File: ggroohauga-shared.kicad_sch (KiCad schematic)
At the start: 13 parts

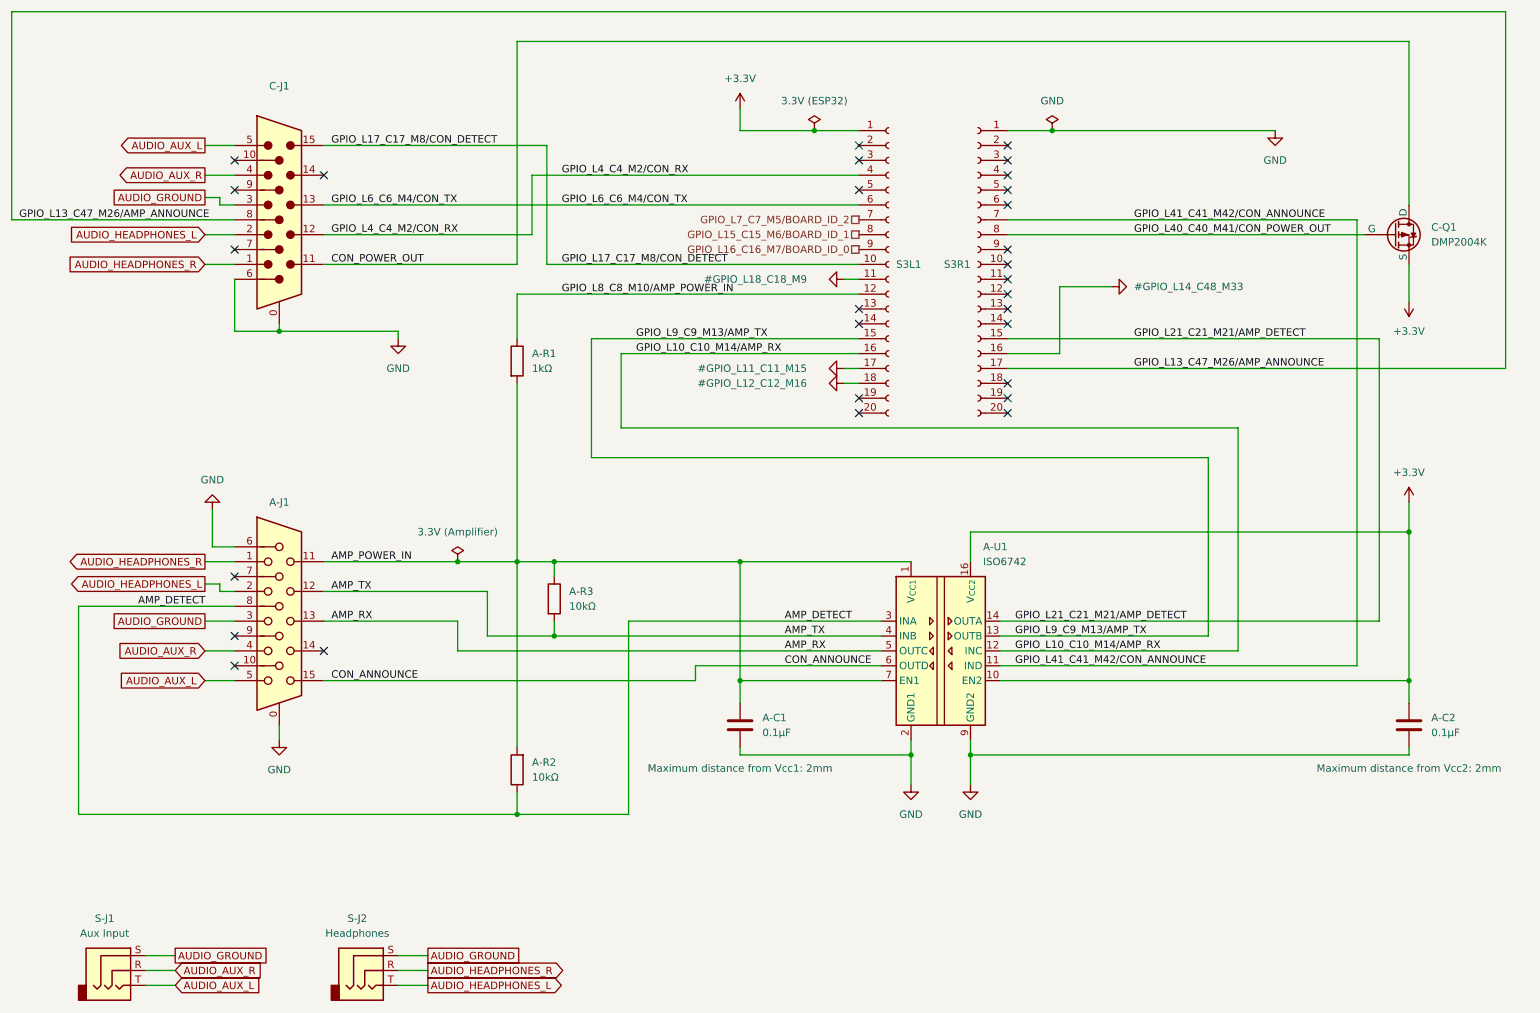
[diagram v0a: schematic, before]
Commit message: Indicate active low signals on the schematic
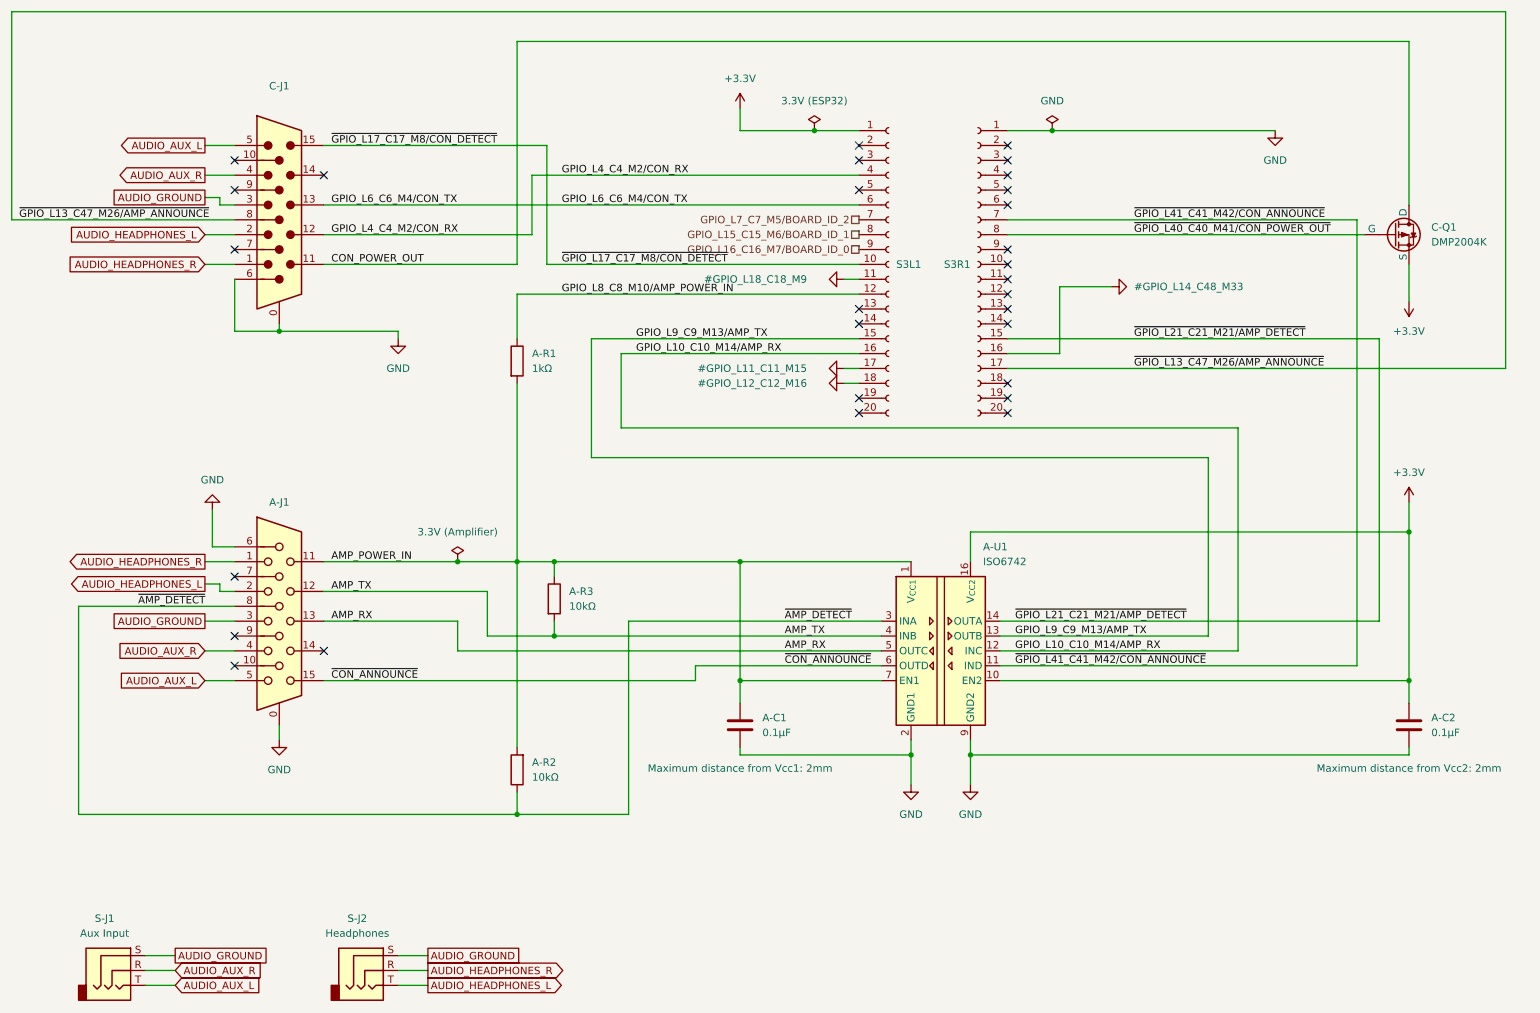
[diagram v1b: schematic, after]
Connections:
- net AMP_DETECT renamed ~{AMP_DETECT}
- net CON_ANNOUNCE renamed ~{CON_ANNOUNCE}
- net GPIO_L13_C47_M26/AMP_ANNOUNCE renamed ~{GPIO_L13_C47_M26/AMP_ANNOUNCE}
- net GPIO_L17_C17_M8/CON_DETECT renamed ~{GPIO_L17_C17_M8/CON_DETECT}
- net GPIO_L21_C21_M21/AMP_DETECT renamed ~{GPIO_L21_C21_M21/AMP_DETECT}
- net GPIO_L40_C40_M41/CON_POWER_OUT renamed ~{GPIO_L40_C40_M41/CON_POWER_OUT}
- net GPIO_L41_C41_M42/CON_ANNOUNCE renamed ~{GPIO_L41_C41_M42/CON_ANNOUNCE}
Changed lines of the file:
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@@
 		)
 	)
-	(label "GPIO_L17_C17_M8{slash}CON_DETECT"
+	(label "~{GPIO_L17_C17_M8{slash}CON_DETECT}"
 		(at 72.39 40.64 0)
 		(effects
@@
 		)
 	)
-	(label "AMP_DETECT"
+	(label "~{AMP_DETECT}"
 		(at 39.37 119.38 0)
 		(effects
@@
 		)
 	)
-	(label "CON_ANNOUNCE"
+	(label "~{CON_ANNOUNCE}"
 		(at 72.39 132.08 0)
 		(effects
@@
 		)
 	)
-	(label "GPIO_L13_C47_M26{slash}AMP_ANNOUNCE"
+	(label "~{GPIO_L13_C47_M26{slash}AMP_ANNOUNCE}"
 		(at 19.05 53.34 0)
 		(effects
@@
 		)
 	)
-	(label "AMP_DETECT"
+	(label "~{AMP_DETECT}"
 		(at 149.86 121.92 0)
 		(effects
@@
 		)
 	)
-	(label "CON_ANNOUNCE"
+	(label "~{CON_ANNOUNCE}"
 		(at 149.86 129.54 0)
 		(effects
@@
 		)
 	)
-	(label "GPIO_L13_C47_M26{slash}AMP_ANNOUNCE"
+	(label "~{GPIO_L13_C47_M26{slash}AMP_ANNOUNCE}"
 		(at 209.55 78.74 0)
 		(effects
@@
 		)
 	)
-	(label "GPIO_L21_C21_M21{slash}AMP_DETECT"
+	(label "~{GPIO_L21_C21_M21{slash}AMP_DETECT}"
 		(at 209.55 73.66 0)
 		(effects
@@
 		)
 	)
-	(label "GPIO_L17_C17_M8{slash}CON_DETECT"
+	(label "~{GPIO_L17_C17_M8{slash}CON_DETECT}"
 		(at 111.76 60.96 0)
 		(effects
@@
 		)
 	)
-	(label "GPIO_L21_C21_M21{slash}AMP_DETECT"
+	(label "~{GPIO_L21_C21_M21{slash}AMP_DETECT}"
 		(at 189.23 121.92 0)
 		(effects
@@
 		)
 	)
-	(label "GPIO_L40_C40_M41{slash}CON_POWER_OUT"
+	(label "~{GPIO_L40_C40_M41{slash}CON_POWER_OUT}"
 		(at 209.55 55.88 0)
 		(effects
@@
 		)
 	)
-	(label "GPIO_L41_C41_M42{slash}CON_ANNOUNCE"
+	(label "~{GPIO_L41_C41_M42{slash}CON_ANNOUNCE}"
 		(at 189.23 129.54 0)
 		(effects
@@
 		)
 	)
-	(label "GPIO_L41_C41_M42{slash}CON_ANNOUNCE"
+	(label "~{GPIO_L41_C41_M42{slash}CON_ANNOUNCE}"
 		(at 209.55 53.34 0)
 		(effects

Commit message: Use the better SOT-23-3 footprint for C-Q1
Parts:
- C-Q1: footprint Package_TO_SOT_SMD:SOT-23 -> Package_TO_SOT_SMD:SOT-23-3
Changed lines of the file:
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@@
 			)
 		)
-		(property "Footprint" "Package_TO_SOT_SMD:SOT-23"
+		(property "Footprint" "Package_TO_SOT_SMD:SOT-23-3"
 			(at 259.08 53.34 0)
 			(effects
